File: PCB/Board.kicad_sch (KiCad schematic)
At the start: 19 parts, among them J1 Screw_Terminal_01x02, J2 Batería, Q1 NPN, Q2 IRLZ44N, Q3 IRF9Z34N, SW1 RotaryEncoder_Switch, U1 ESP32-C3-SuperMini, U2 LM7805_TO220

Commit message: update: PCB SCH
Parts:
- added BZ1: Buzzer_5V, Buzzer_Beeper:MagneticBuzzer_ProSignal_ABT-410-RC, symbol PCM_SL_Devices:Buzzer_5V
- added J3: 2.42In OLED, Connector_PinHeader_2.54mm:PinHeader_1x04_P2.54mm_Vertical, symbol Connector_Generic:Conn_01x04
- J1: footprint (none) -> TerminalBlock:TerminalBlock_MaiXu_MX126-5.0-02P_1x02_P5.00mm
- Q1: footprint (none) -> Package_TO_SOT_THT:TO-92L_HandSolder
- R1, R2, R3: footprint (none) -> Resistor_THT:R_Axial_DIN0207_L6.3mm_D2.5mm_P10.16mm_Horizontal
- R5: value 1R 5/10W -> 1R 5W
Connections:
- net CHG_PWM: now also U1.9 (GPIO5)
- net DCH_PWM: now also U1.14 (GPIO10)
- net GND: now also J3.1 (Pin_1)
- net VCC: now also J3.2 (Pin_2)
- net TEMP_ADC: now reaches U1.1 (GPIO0)
- net BUZZER: now reaches U1.15 (GPIO20)
- net ENC_CLK: now reaches U1.2 (GPIO1)
- net ENC_DT: now reaches U1.4 (GPIO3)
- net ENC_SW: now reaches U1.5 (GPIO4)
- new net SCL: J3.3 (Pin_3)
- new net SDA: J3.4 (Pin_4)
- no-connect marks 0 -> 6
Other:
- moved on the sheet: J1, U2

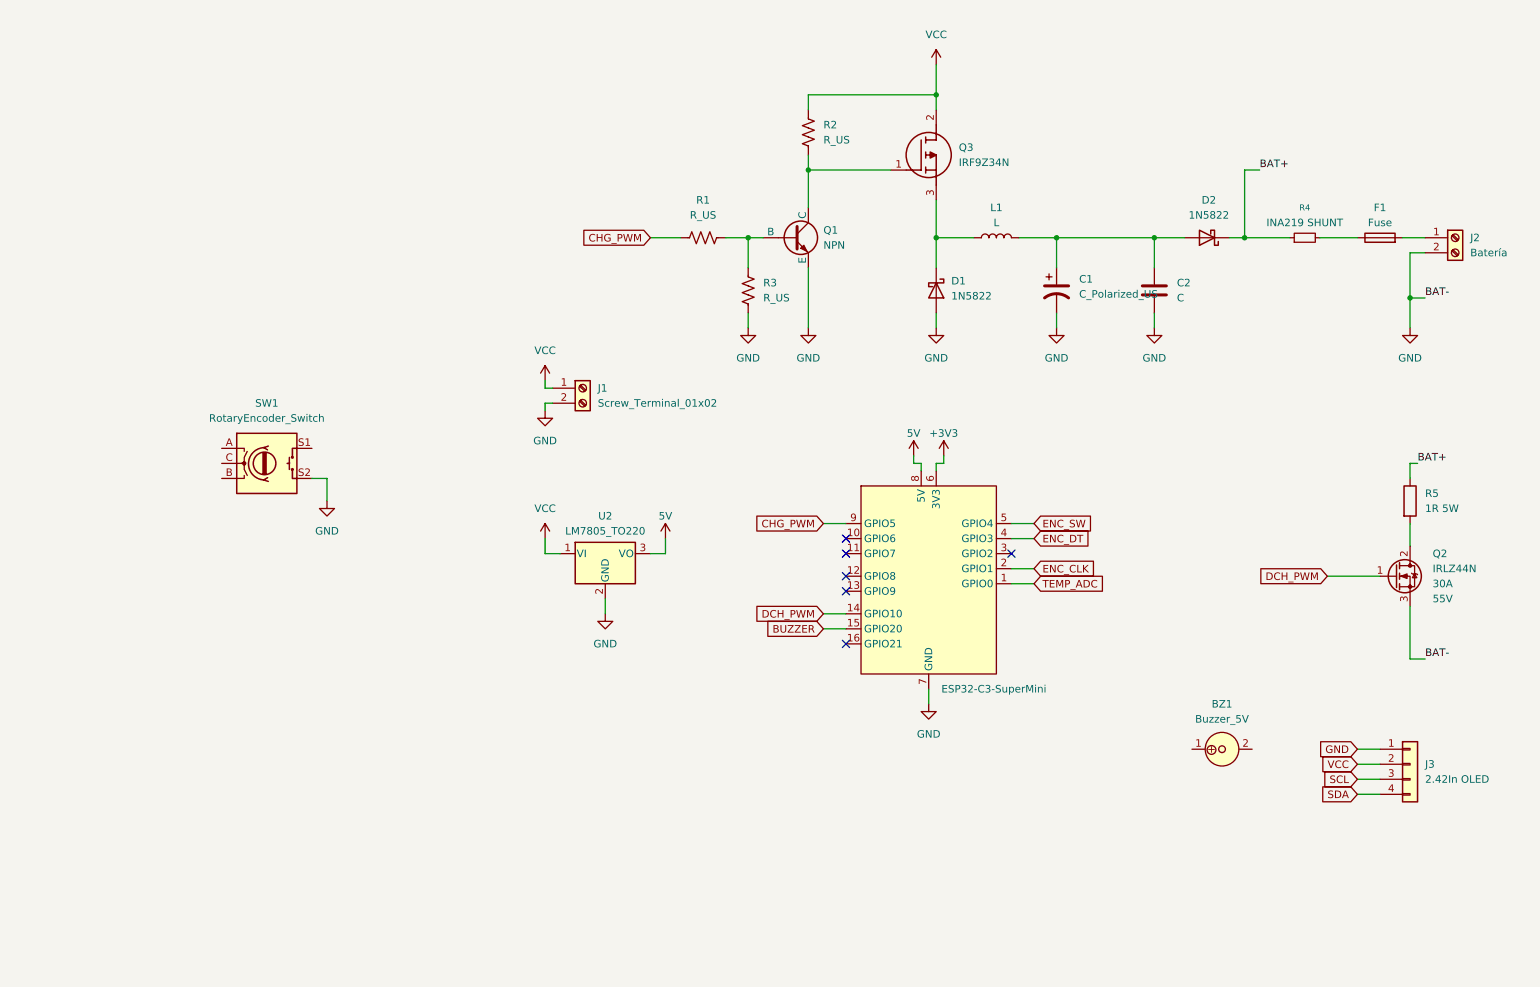
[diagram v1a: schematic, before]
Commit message: Added: Especificacion de los componentes del buck
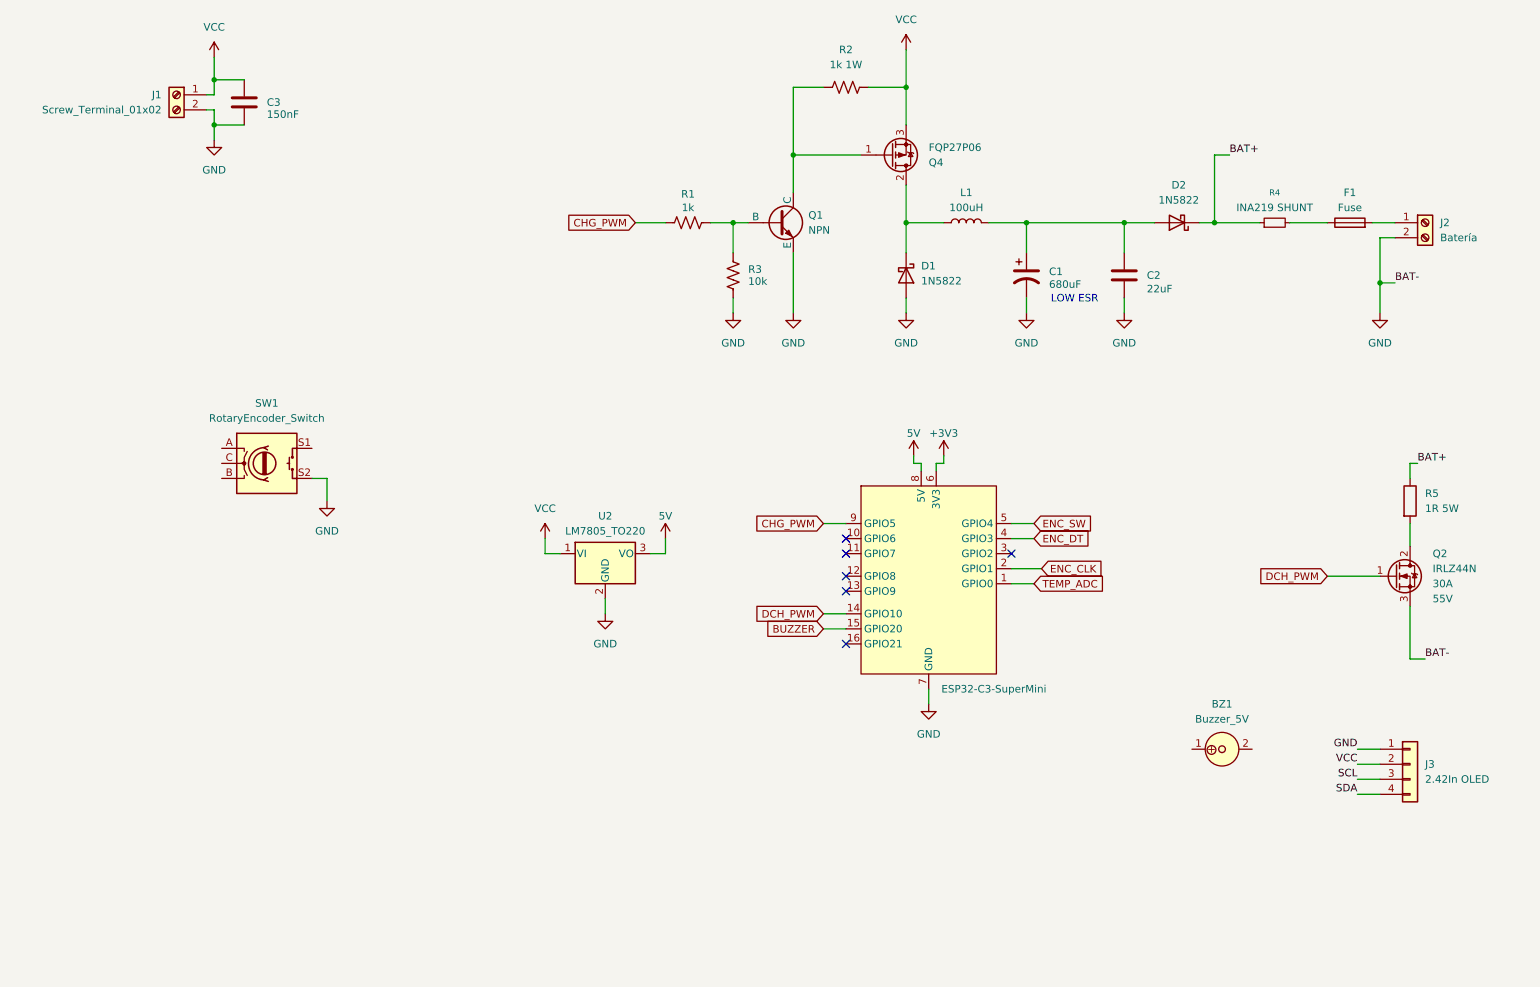
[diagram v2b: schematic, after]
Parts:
- removed Q3: IRF9Z34N, PCM_IRF9Z34N:TO254P469X1042X1967-3P, symbol PCM_IRF9Z34N:IRF9Z34N
- added C3: 150nF, symbol Device:C
- added Q4: FQP27P06, Package_TO_SOT_THT:TO-220-3_Vertical, symbol Transistor_FET:FQP27P06
- C1: value C_Polarized_US -> 680uF
- C2: value C -> 22uF
- L1: value L -> 100uH
- R1: value R_US -> 1k
- R2: value R_US -> 1k 1W
- R3: value R_US -> 10k
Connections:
- net GND: now also C3.2
- net VCC: now also C3.1, Q4.3 (S)
- net at Q1.1 (C), R2.2: now also Q4.1 (G)
- net at D1.1 (K), L1.1: now also Q4.2 (D)
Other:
- note added: "LOW ESR"
- moved on the sheet: C1, C2, D1, D2, F1, J1, J2, L1, Q1, R1, R2, R3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
